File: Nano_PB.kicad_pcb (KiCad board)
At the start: 2 copper layers, 100 x 50 mm, 143 parts, among them CON1 BARREL_JACK, P1 CONN_02X04, P10 CONN_01X04, P11 CONN_01X04, P12 CONN_01X04, P13 CONN_01X01, P14 CONN_01X01, P15 CONN_01X01, P16 CONN_01X01, P17 CONN_01X01, P2 CONN_01X06, P3 CONN_01X01, P4 CONN_01X03, P5 CONN_01X03, P6 CONN_01X03, P7 CONN_01X03, P8 CONN_01X03, P9 CONN_01X04, Q1 SMBT3904, Q2 SMBT3904, Q3 SMBT3904, Q4 SMBT3904, Q5 SMBT3904, Q6 BSS138, Q7 BSS138, Q8 SMBT3904, Q9 SMBT3904, SW1 Izquierda, SW2 Arriba, SW3 Abajo, SW4 Derecha, U1 Arduino_Nano, U2 LM7805CT, U3 MCP23017, U5 Matriz_5x7, U6 PCA9551, U8 MMA7660FC, U9 40106

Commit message: version definitiva V0.4
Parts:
- removed the Gnd-Via at (137.9, 27.3)
- removed the Gnd-Via at (137.9, 30.7)
- removed the Gnd-Via at (137.9, 34.0)
- removed the Gnd-Via at (137.9, 37.2)
- added Gnd-Via: VAL**, Vias:Gnd-Via, F.Cu at (73.7, 47.9)
- added Gnd-Via: VAL**, Vias:Gnd-Via, F.Cu at (80.0, 50.0)
- added Gnd-Via: VAL**, Vias:Gnd-Via, F.Cu at (84.2, 52.4)
- moved Gnd-Via 2.95 mm to (55.2, 39.6)
- moved REF** 0.96 mm to (54.6, 32.5)
- moved R13 0.82 mm to (101.3, 34.6)
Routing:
- net +5V: track 438.2 -> 465.6 mm
- net D11: track 49.1 -> 48.3 mm
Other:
- board text added: "Key"

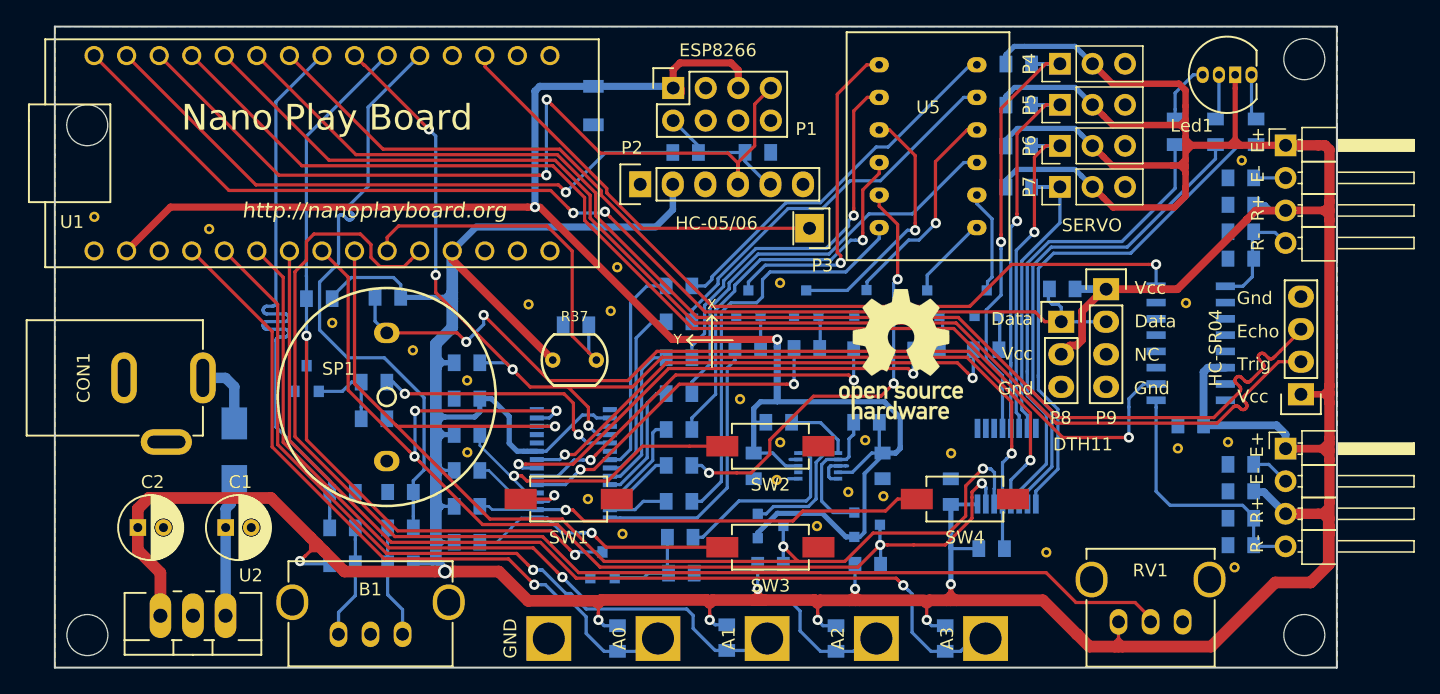
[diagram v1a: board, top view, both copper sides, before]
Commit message: cambiadas huellas erroneas en U3 y U9. Corrige issues #17 y #18
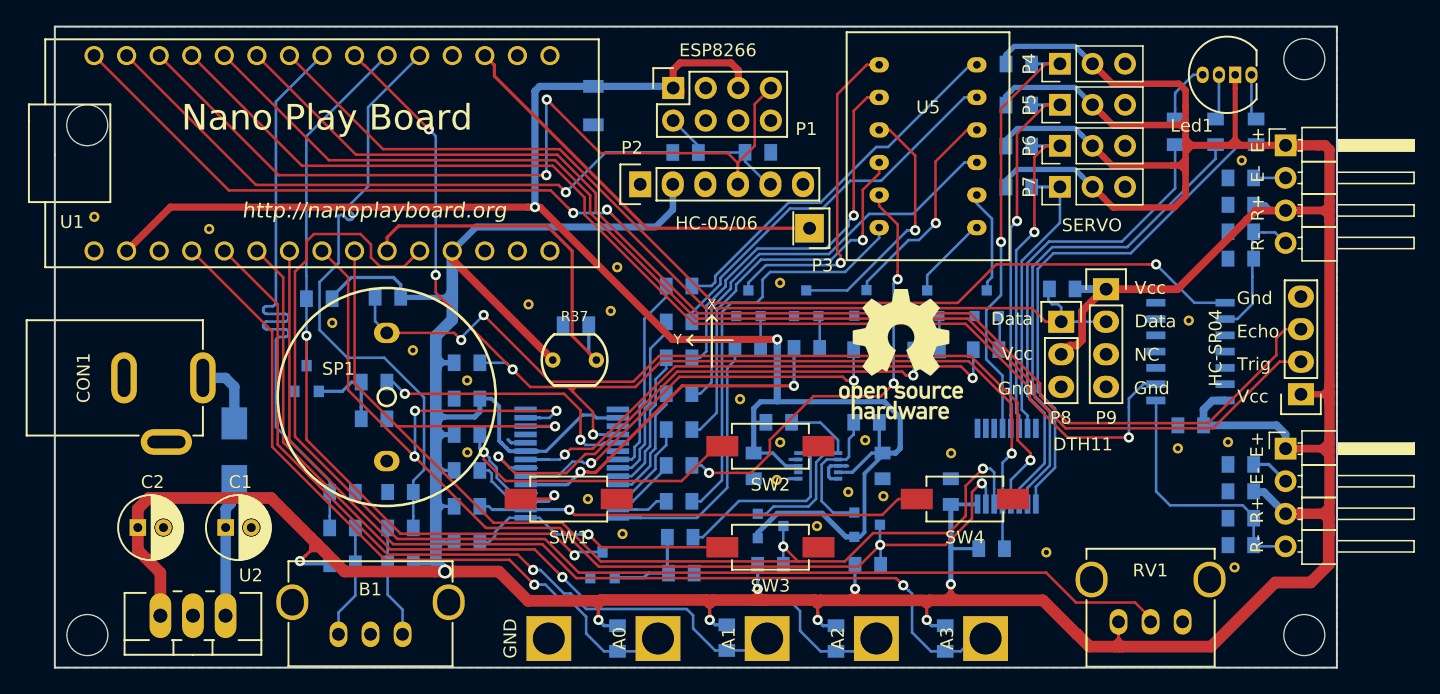
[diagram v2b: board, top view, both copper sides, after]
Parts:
- U3: footprint Housings_SSOP:TSSOP-28_4.4x9.7mm_Pitch0.65mm -> Housings_SSOP:SSOP-28_5.3x10.2mm_Pitch0.65mm
- U9: footprint Housings_SOIC:SOIC-16_3.9x9.9mm_Pitch1.27mm -> Housings_SOIC:SOIC-14_3.9x8.7mm_Pitch1.27mm
- moved Gnd-Via 1.39 mm to (140.5, 47.7)
- moved U9 0.65 mm to (140.7, 50.1)
- moved U3 0.13 mm to (92.4, 58.9)
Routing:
- net PB1: track 35.3 -> 40.9 mm
- net PB6: track 37.5 -> 42.9 mm
- net D6: track 79.0 -> 83.5 mm
- net PB3: track 24.6 -> 28.4 mm
- net PB2: track 9.74 -> 13.0 mm
- net PB4: track 26.1 -> 29.3 mm
- net PB5: track 30.6 -> 33.1 mm
- net Net-(C18-Pad1): track 8.92 -> 11.2 mm
- net A5: track 91.6 -> 93.8 mm
- net PA7: track 21.2 -> 23.0 mm
- net +5V: track 465.6 -> 463.8 mm
- net PB7: track 39.8 -> 41.4 mm
- net D7: track 100.0 -> 98.5 mm
- net GND: track 4.67 -> 6.16 mm
- net PA6: track 4.66 -> 6.13 mm
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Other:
- net class Default: clearance 0.1778 -> 0.2032; trace_width 0.254 -> 0.2032
- net class Power: clearance 0.3048 -> 0.254
- rule trace_clearance: 0.1778 -> 0.2032
- board text added: "03/17"
- board text added: "Rev-0.4.1"
- board text removed: "01/17"
- board text removed: "Rev-0.4.0"

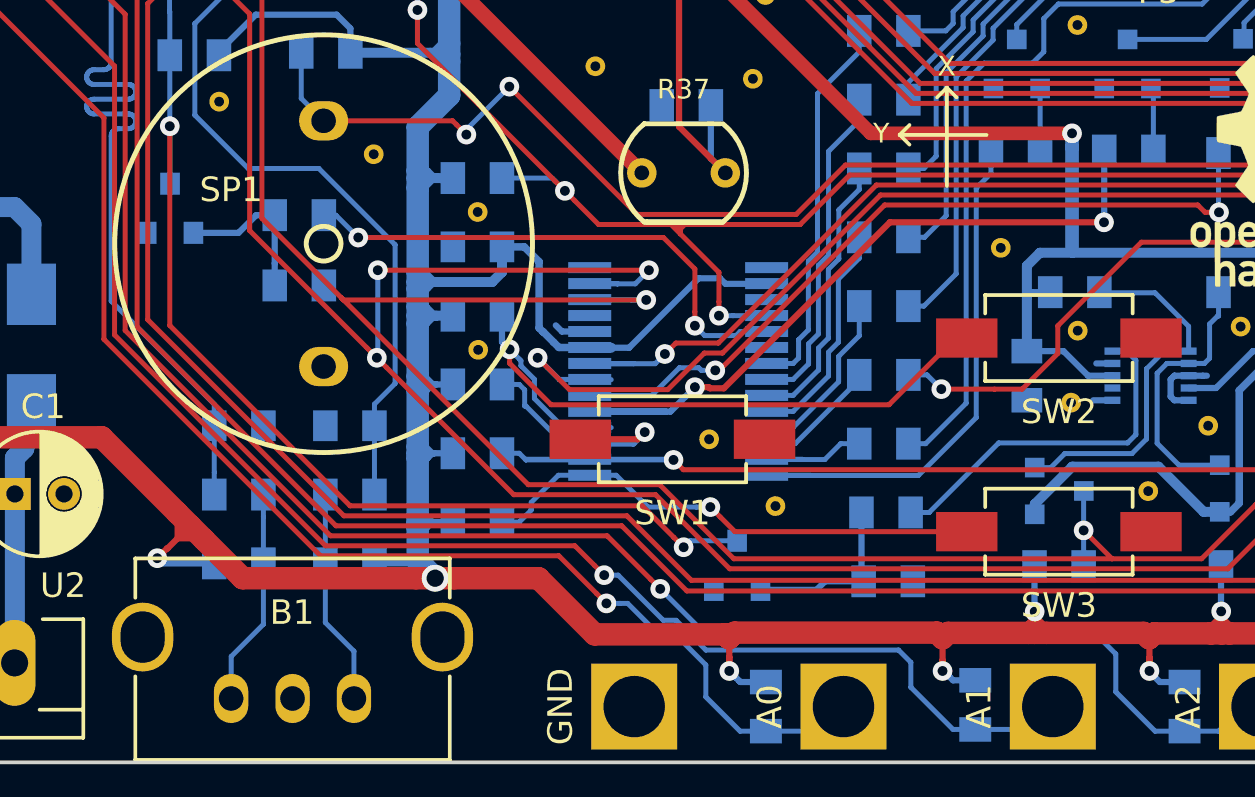
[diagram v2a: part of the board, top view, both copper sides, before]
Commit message: modificar posicion de vias de alimentacion proximas al chasis del encoder
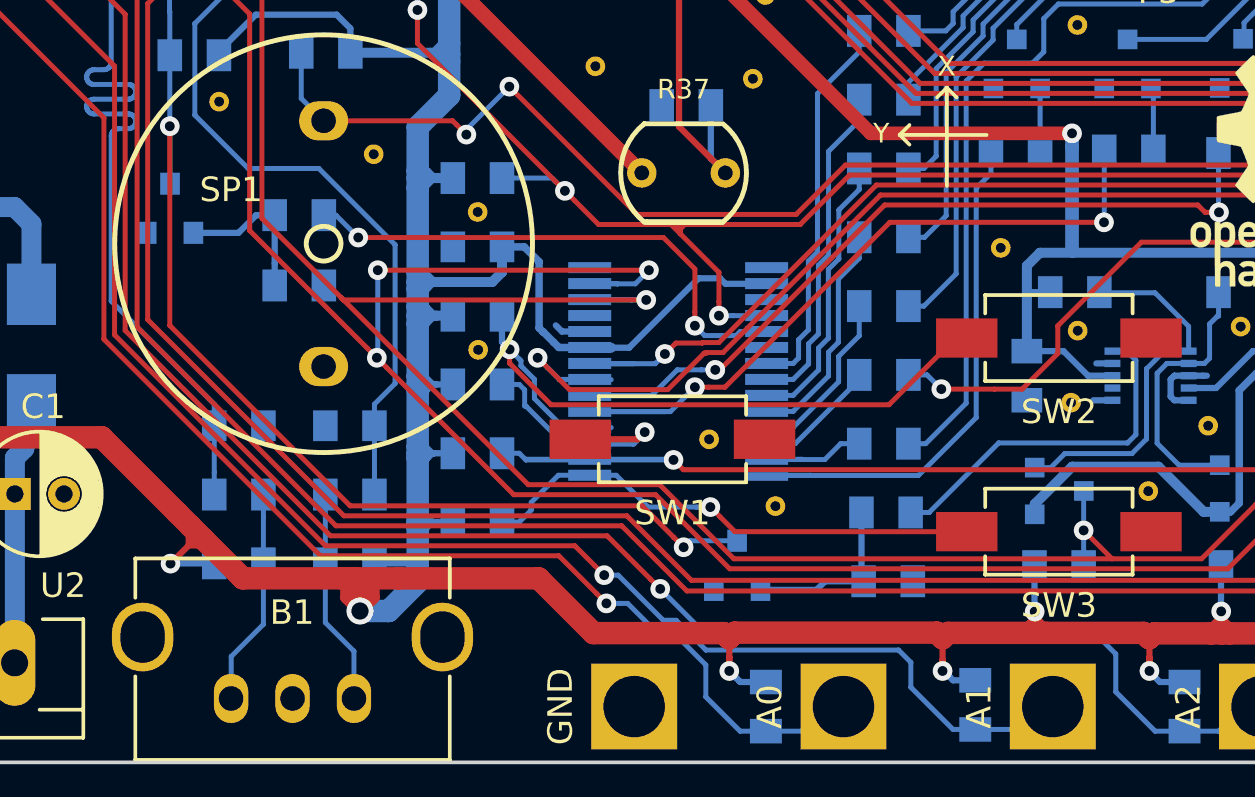
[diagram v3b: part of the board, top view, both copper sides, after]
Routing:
- net +5V: track 463.8 -> 470.1 mm

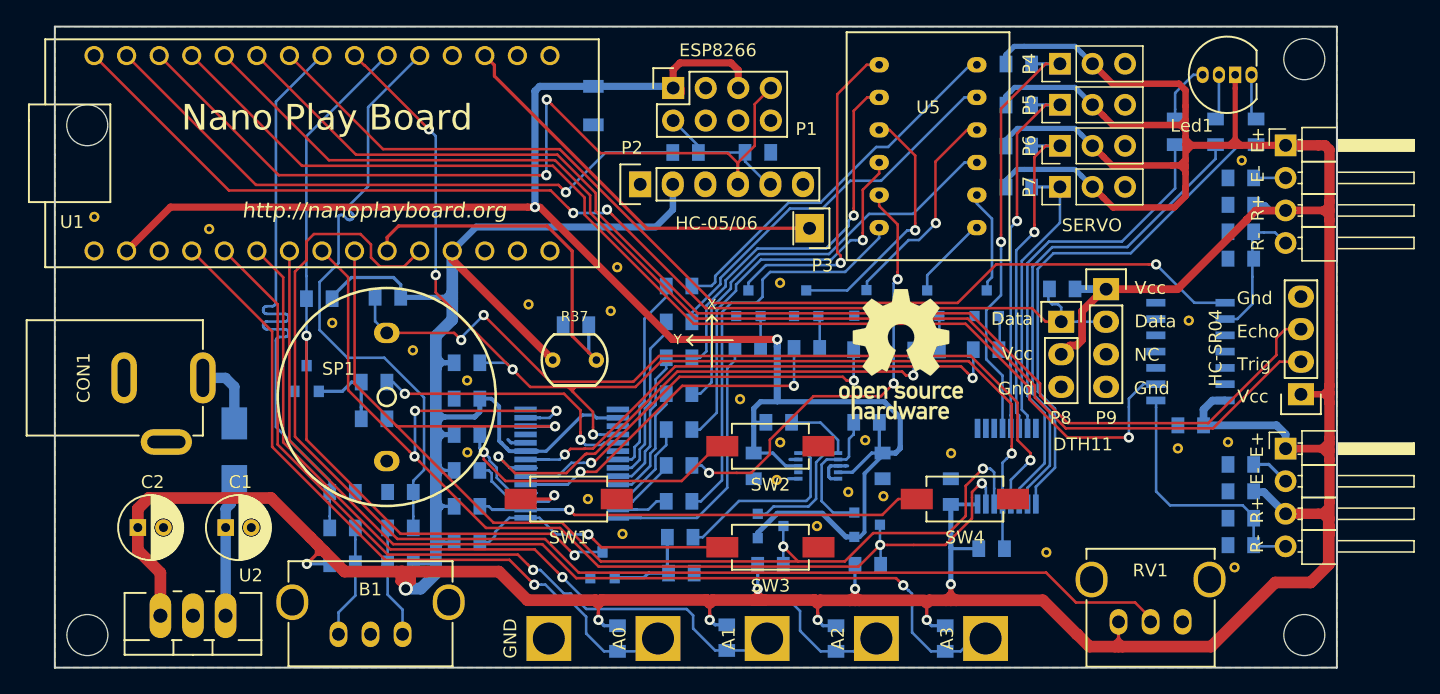
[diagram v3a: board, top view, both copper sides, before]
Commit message: finalizada V0.4.1 corrige #17, #18 y #19
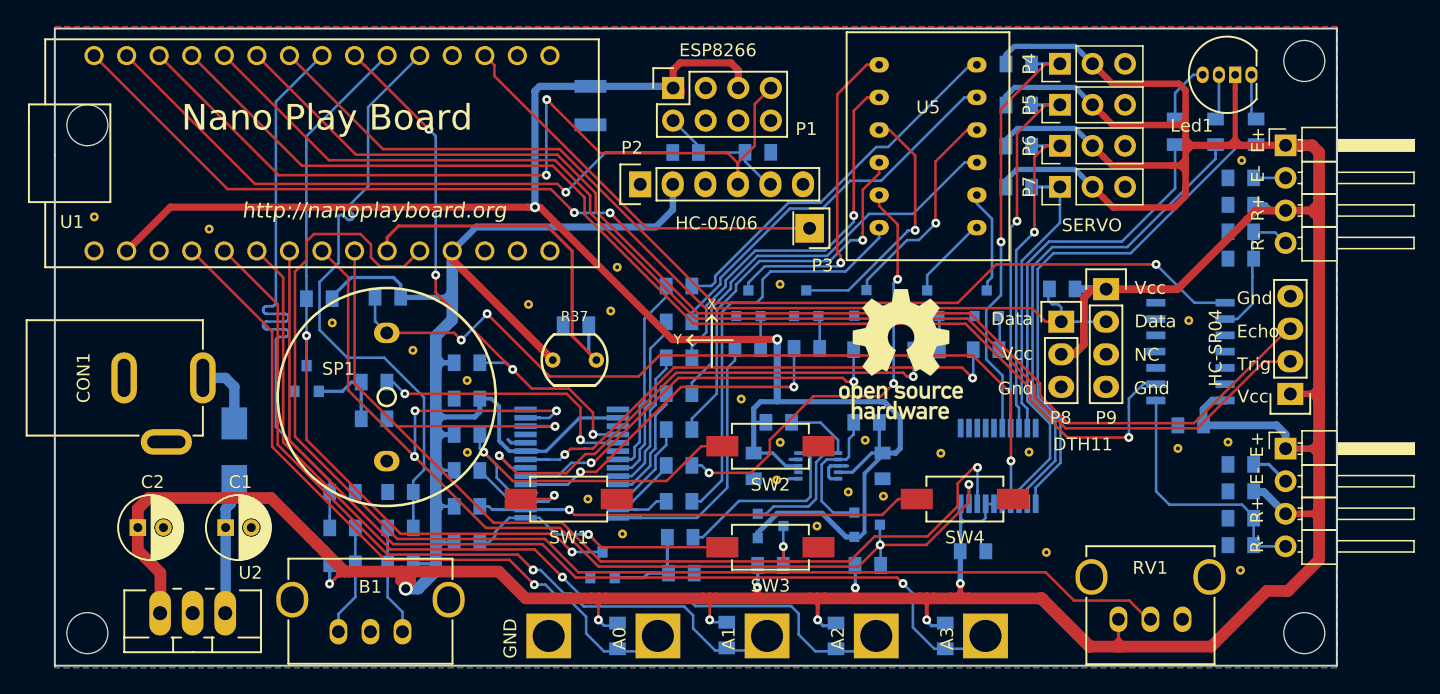
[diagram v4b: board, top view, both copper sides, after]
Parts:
- removed R15: 10K, Resistencias:R_0805
- added Gnd-Via: VAL**, Vias:Gnd-Via, F.Cu at (128.1, 58.0)
- C15, C16: value 1u -> 100n
- C5: footprint Capacitors_SMD:C_1206 -> Capacitors_SMD:C_1210
- R40, R42: value 10K -> 1K
- U6: value PCA9551 -> PCA9634; footprint Housings_SSOP:TSSOP-16_4.4x5mm_Pitch0.65mm -> Housings_SSOP:TSSOP-20_4.4x6.5mm_Pitch0.65mm
- moved C7 4.96 mm to (123.7, 65.7), turned to 0 degrees
- moved P10 0.83 mm to (148.5, 53.4)
- moved Gnd-Via 0.80 mm to (121.2, 58.0)
- moved U6 0.67 mm to (125.7, 59.0)
- moved Gnd-Via 0.51 mm to (144.6, 67.2)
- moved C5 0.23 mm to (93.9, 30.9)
- moved U2 0.20 mm to (62.8, 70.5)
- moved P13 0.20 mm to (99.1, 72.3)
- moved P14 0.20 mm to (107.6, 72.3)
- moved P15 0.20 mm to (116.2, 72.3)
- moved P17 0.20 mm to (90.6, 72.3)
- moved P16 0.20 mm to (124.7, 72.3)
- moved RV1 0.20 mm to (137.6, 71.0)
- moved B1 0.20 mm to (76.7, 72.0)
- moved R28 0.20 mm to (96.0, 72.3)
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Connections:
- U6 pad 10: LED_BLUE -> GND
- U6 pad 11: LED_GREEN -> LED_RED
- U6 pad 12: BUZZER -> LED_BLUE
- U6 pad 13: ~RESET -> LED_GREEN
- U6 pad 14: A5 -> BUZZER
- U6 pad 15: A4 -> GND
- U6 pad 4: SERVO1 -> GND
- U6 pad 5: SERVO2 -> GND
- U6 pad 6: SERVO3 -> SERVO1
- U6 pad 7: SERVO4 -> SERVO2
- U6 pad 8: GND -> SERVO3
- U6 pad 9: LED_RED -> SERVO4
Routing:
- net ~RESET: track 92.6 -> 43.1 mm, vias 5 -> 4
- net +5V: track 470.1 -> 473.8 mm
- net PB6: track 42.9 -> 40.8 mm
- net A4: track 93.5 -> 91.7 mm
- net D7: track 98.5 -> 96.9 mm
- net BUZZER: track 67.0 -> 65.5 mm
- net D8: track 99.6 -> 99.1 mm
- net +3V3: track 137.9 -> 138.5 mm
- net A5: track 93.8 -> 93.3 mm
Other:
- board size 100 x 50 mm -> 100 x 49.7 mm
- rule pad_to_mask_clearance: 0.1778 -> 0.14
